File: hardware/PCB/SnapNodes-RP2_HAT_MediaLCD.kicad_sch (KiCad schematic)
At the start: 43 parts, among them J20 Conn_01x24_MountingPin

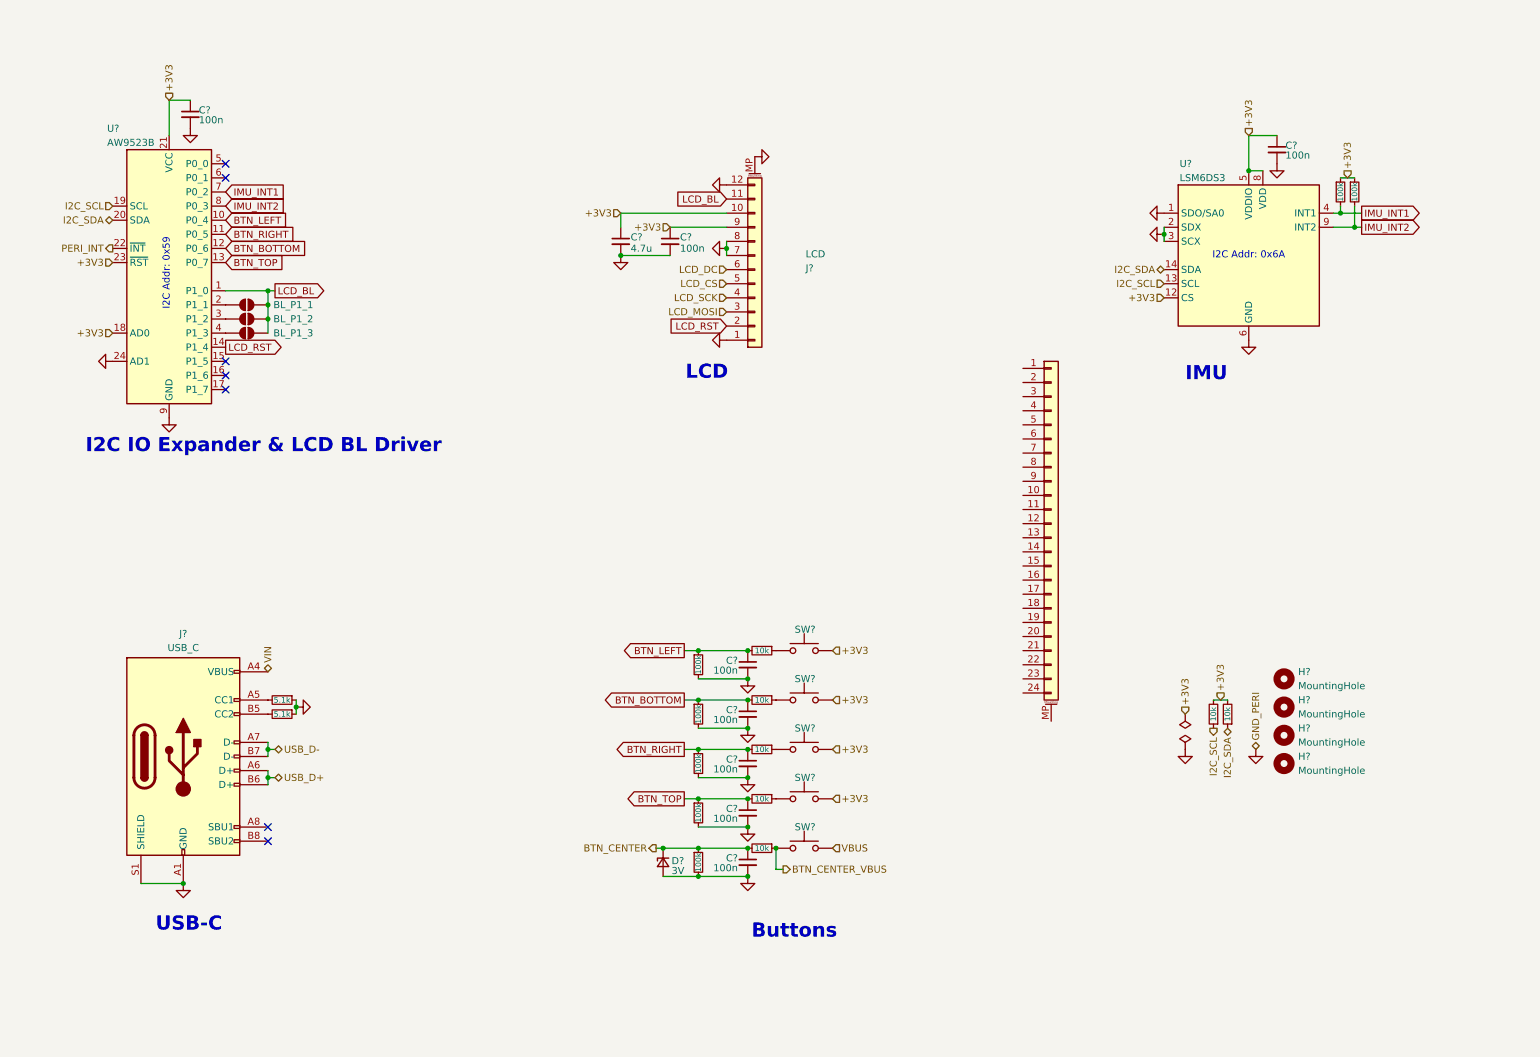
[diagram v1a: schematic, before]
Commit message: HAT V2 PCB done, minor fix for Core PCB
Signed-off-by: Hanxiang Chen <jhxchen7@outlook.com>
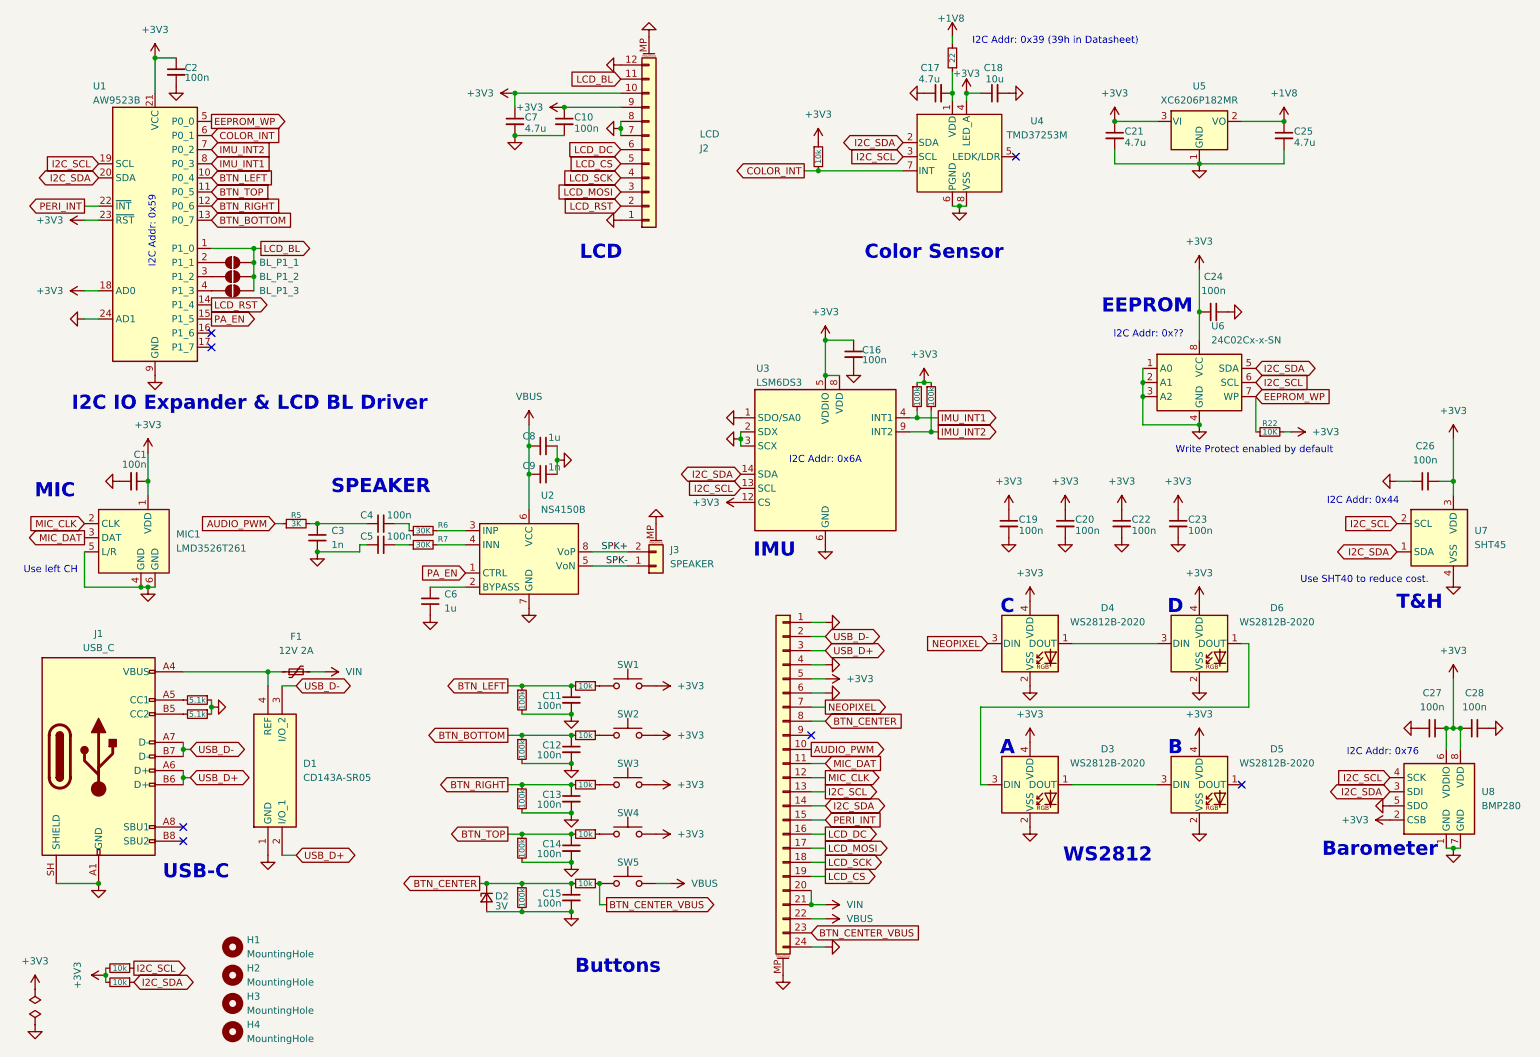
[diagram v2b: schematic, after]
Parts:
- added C1, C19, C20, C22, C23, C24, C26, C27, C28, C4, C5: 100n, Capacitor_SMD:C_0603_1608Metric, symbol Device:C_Small
- added C17, C21, C25: 4.7u, Capacitor_SMD:C_0603_1608Metric, symbol Device:C_Small
- added C18: 10u, Capacitor_SMD:C_0603_1608Metric, symbol Device:C_Small
- added C3, C9: 1n, Capacitor_SMD:C_0603_1608Metric, symbol Device:C_Small
- added C6, C8: 1u, Capacitor_SMD:C_0603_1608Metric, symbol Device:C_Small
- added D1: CD143A-SR05, Package_TO_SOT_SMD:SOT-143, symbol CD143A-SR05:CD143A-SR05
- added D3, D4, D5, D6: WS2812B-2020, LED_SMD:LED_WS2812B-2020_PLCC4_2.0x2.0mm, symbol LED:WS2812B-2020
- added F1: 12V 2A, Fuse:Fuse_0805_2012Metric, symbol Device:Polyfuse_Small
- added J3: SPEAKER, Connector_Molex:Molex_PicoBlade_53261-0271_1x02-1MP_P1.25mm_Horizontal, symbol Connector_Generic_MountingPin:Conn_01x02_MountingPin
- added MIC1: LMD3526T261, Project:MIC-SMD_6P-L3.5-W2.7-P0.884-TR, symbol Project:LMD3526T261
- added R18: 10k, Resistor_SMD:R_0603_1608Metric, symbol Device:R_Small
- added R21: 22, Resistor_SMD:R_0603_1608Metric, symbol Device:R_Small
- added R22: 10K, Resistor_SMD:R_0603_1608Metric, symbol Device:R_Small
- added R5: 3K, Resistor_SMD:R_0603_1608Metric, symbol Device:R_Small
- added R6, R7: 30K, Resistor_SMD:R_0603_1608Metric, symbol Device:R_Small
- added U2: NS4150B, Package_SO:MSOP-8_3x3mm_P0.65mm, symbol Project:NS4150B
- added U4: TMD37253M, Project:LGA8_TMD37253_OSM, symbol TMD37253M:TMD37253M
- added U5: XC6206P182MR, Package_TO_SOT_SMD:SOT-23-3, symbol Regulator_Linear:XC6206PxxxMR
- added U6: 24C02Cx-x-SN, Package_SO:SOIC-8_3.9x4.9mm_P1.27mm, symbol Memory_EEPROM:24C02Cx-x-SN
- added U7: SHT45, Sensor_Humidity:Sensirion_DFN-4_1.5x1.5mm_P0.8mm_SHT4x_NoCentralPad, symbol Sensor_Humidity:SHT4x
- added U8: BMP280, Package_LGA:Bosch_LGA-8_2x2.5mm_P0.65mm_ClockwisePinNumbering, symbol Sensor_Pressure:BMP280
- JP1, JP2, JP3: renamed from JP?; footprint Jumper:SolderJumper-2_P1.3mm_Open_TrianglePad1.0x1.5mm -> Jumper:SolderJumper-2_P1.3mm_Open_RoundedPad1.0x1.5mm
- U1: renamed from U?; footprint Package_DFN_QFN:QFN-24-1EP_4x4mm_P0.5mm_EP2.7x2.7mm -> Package_DFN_QFN:QFN-24-1EP_4x4mm_P0.5mm_EP2.7x2.7mm_ThermalVias
- gave numbers to parts that had none: 38
- renumbered J20 to J4
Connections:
- net +3V3: now also J4.5 (Pin_5), C1.1, C18.1, C19.1, C20.1, C21.1, C22.1, C23.1, C24.1, C26.2, C27.2, C28.1, D3.4 (VDD), D4.4 (VDD), D5.4 (VDD), D6.4 (VDD), MIC1.1 (VDD), R18.1, R22.2, U4.4 (LED_A), U5.3 (VI), U6.8 (VCC), U7.3 (VDD), U8.2 (CSB), U8.6 (VDDIO), U8.8 (VDD)
- net BTN_BOTTOM: now also U1.13 (P0_7); no longer U1.12 (P0_6)
- net BTN_CENTER: now also J4.8 (Pin_8)
- net BTN_CENTER_VBUS: now also J4.23 (Pin_23)
- net BTN_RIGHT: now also U1.12 (P0_6); no longer U1.11 (P0_5)
- net BTN_TOP: now also U1.11 (P0_5); no longer U1.13 (P0_7)
- net I2C_SCL: now also J4.13 (Pin_13), R1.1, U4.3 (SCL), U6.6 (SCL), U7.2 (SCL), U8.4 (SCK); no longer R2.1
- net I2C_SDA: now also J4.14 (Pin_14), R2.1, U4.2 (SDA), U6.5 (SDA), U7.1 (SDA), U8.3 (SDI); no longer R1.1
- net IMU_INT1: now also U1.8 (P0_3); no longer U1.7 (P0_2)
- net IMU_INT2: now also U1.7 (P0_2); no longer U1.8 (P0_3)
- net LCD_CS: now also J4.19 (Pin_19)
- net LCD_DC: now also J4.16 (Pin_16)
- net LCD_MOSI: now also J4.17 (Pin_17)
- net LCD_SCK: now also J4.18 (Pin_18)
- net PERI_INT: now also J4.15 (Pin_15)
- net USB_D+: now also J4.3 (Pin_3), D1.2 (I/O_1)
- net USB_D-: now also J4.2 (Pin_2), D1.3 (I/O_2)
- net VBUS: now also J4.22 (Pin_22), C8.2, C9.2, U2.6 (VCC)
- net VIN: now also J4.20 (Pin_20), J4.21 (Pin_21), F1.2; no longer J1.A4 (VBUS), J1.A9 (VBUS), J1.B4 (VBUS), J1.B9 (VBUS)
- net GND: now reaches J4.1 (Pin_1)
- net GND: now also C10.2, C11.2, C12.2, C13.2, C14.2, C15.2, C16.2, C2.2, C7.2, D2.2 (A), J1.A1 (GND), J1.A12 (GND), J1.B1 (GND), J1.B12 (GND), J1.SH (SHIELD), J2.1 (Pin_1), J2.12 (Pin_12), J2.7 (Pin_7), J2.8 (Pin_8), J2.MP (MountPin), J4.24 (Pin_24), J4.4 (Pin_4), J4.6 (Pin_6), J4.MP (MountPin), R10.2, R11.2, R12.2, R3.1, R4.1, R8.2, R9.2, U1.24 (AD1), U1.25 (GND), U1.9 (GND), U3.1 (SDO/SA0), U3.2 (SDX), U3.3 (SCX), U3.6 (GND), U3.7 (GND), C1.2, C17.1, C18.2, C19.2, C20.2, C21.2, C22.2, C23.2, C24.2, C25.2, C26.1, C27.1, C28.2, C3.1, C5.1, C6.1, C8.1, C9.1, D1.1 (GND), D3.2 (VSS), D4.2 (VSS), D5.2 (VSS), D6.2 (VSS), J3.MP (MountPin), MIC1.4 (GND), MIC1.5 (L/R), MIC1.6 (GND), U2.7 (GND), U4.6 (PGND), U4.8 (VSS), U5.1 (GND), U6.1 (A0), U6.2 (A1), U6.3 (A2), U6.4 (GND), U7.4 (VSS), U8.1 (GND), U8.5 (SDO), U8.7 (GND)
- net AUDIO_PWM: now reaches J4.10 (Pin_10)
- net AUDIO_PWM: now also R5.1
- net MIC_DAT: now reaches J4.11 (Pin_11)
- net MIC_DAT: now also MIC1.3 (DAT)
- net MIC_CLK: now reaches J4.12 (Pin_12)
- net MIC_CLK: now also MIC1.2 (CLK)
- net NEOPIXEL: now reaches J4.7 (Pin_7)
- net NEOPIXEL: now also D4.3 (DIN)
- net PA_EN: now reaches U1.15 (P1_5)
- net PA_EN: now also U2.1 (CTRL)
- net EEPROM_WP: now reaches U1.5 (P0_0)
- net EEPROM_WP: now also R22.1, U6.7 (WP)
- net COLOR_INT: now reaches U1.6 (P0_1)
- net COLOR_INT: now also R18.2, U4.7 (INT)
- removed net GND_PERI: C10.2, C11.2, C12.2, C13.2, C14.2, C15.2, C16.2, C2.2, C7.2, D2.2 (A), J1.A1 (GND), J1.A12 (GND), J1.B1 (GND), J1.B12 (GND), J1.S1 (SHIELD), J2.1 (Pin_1), J2.12 (Pin_12), J2.7 (Pin_7), J2.8 (Pin_8), J2.MP (MountPin), R10.2, R11.2, R12.2, R3.1, R4.1, R8.2, R9.2, U1.24 (AD1), U1.25 (GND), U1.9 (GND), U3.1 (SDO/SA0), U3.2 (SDX), U3.3 (SCX), U3.6 (GND), U3.7 (GND)
- new net: C5.2, R7.1
- new net: D1.4 (REF), F1.1, J1.A4 (VBUS), J1.A9 (VBUS), J1.B4 (VBUS), J1.B9 (VBUS)
- new net: D4.1 (DOUT), D6.3 (DIN)
- new net: D3.1 (DOUT), D5.3 (DIN)
- new net: D3.3 (DIN), D6.1 (DOUT)
- new net: C17.2, R21.1, U4.1 (VDD)
- new net: C6.2, U2.2 (BYPASS)
- new net: C3.2, C4.1, R5.2
- new net: C4.2, R6.1
- new net: R6.2, U2.3 (INP)
- new net: R7.2, U2.4 (INN)
- new net +1V8: C25.1, R21.2, U5.2 (VO)
- new net SPK+: J3.2 (Pin_2), U2.8 (VoP)
- new net SPK-: J3.1 (Pin_1), U2.5 (VoN)
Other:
- note added: "A"
- note added: "B"
- note added: "Barometer"
- note added: "C"
- note added: "Color Sensor"
- note added: "D"
- note added: "EEPROM"
- note added: "I2C Addr: 0x39 (39h in Datasheet)"
- note added: "I2C Addr: 0x44"
- note added: "I2C Addr: 0x76"
- note added: "I2C Addr: 0x??"
- note added: "MIC"
- note added: "SPEAKER"
- note added: "T&H"
- note added: "Use SHT40 to reduce cost."
- note added: "Use left CH"
- note added: "WS2812"
- note added: "Write Protect enabled by default"
- company: (none) -> shBLOCK & Jason Chen
- title: (none) -> SnapNode-RP2 Hat
- moved on the sheet: C10, C11, C12, C13, C14, C15, C16, C2, C7, D2, H1, H2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

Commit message: all V2 PCBs done
Signed-off-by: Hanxiang Chen <jhxchen7@outlook.com>
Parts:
- removed C9: 1n, Capacitor_SMD:C_0603_1608Metric, symbol Device:C_Small
- C1, C10, C11, C12, C13, C14, C15, C16, C19, C2, C20, C22, C23, C24, C26, C27, C28, C4, C5: LCSC P/N (none) -> C14663
- C17, C21, C25, C7: LCSC P/N (none) -> C19666
- C18: LCSC P/N (none) -> C19702
- C3: LCSC P/N (none) -> C1588
- C6, C8: LCSC P/N (none) -> C15849
- D1: LCSC P/N (none) -> C521962
- D2: LCSC P/N (none) -> C2910134
- D3, D4, D5, D6: LCSC P/N (none) -> C52917434
- F1: LCSC P/N (none) -> C48783161
- J1: LCSC P/N (none) -> C2765186
- J2: LCSC P/N (none) -> C49274051
- J3: LCSC P/N (none) -> C53477378
- J4: LCSC P/N (none) -> C481246
- MIC1: LCSC P/N (none) -> C49230436
- R1, R13, R14, R15, R16, R17, R18, R2, R22: LCSC P/N (none) -> C25804
- R10, R11, R12, R19, R20, R8, R9: LCSC P/N (none) -> C25803
- R21: LCSC P/N (none) -> C23345
- R3, R4: LCSC P/N (none) -> C23186
- R5: LCSC P/N (none) -> C4211
- R6, R7: LCSC P/N (none) -> C22984
- U1: LCSC P/N (none) -> C148077
- U2: LCSC P/N (none) -> C189961
- U3: LCSC P/N (none) -> C95230
- U4: LCSC P/N (none) -> C2153068
- U5: LCSC P/N (none) -> C347373
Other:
- title: SnapNode-RP2 Hat -> SnapNodes-RP2 Hat
